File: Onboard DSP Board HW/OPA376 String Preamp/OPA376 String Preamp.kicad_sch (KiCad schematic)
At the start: 4 parts

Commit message: WIP
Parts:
- removed J9: (no value), Connector_JST:JST_SH_SM06B-SRSS-TB_1x06-1MP_P1.00mm_Horizontal, symbol Connector:Conn_01x07_Socket
- added J9: (no value), Connector_PinHeader_2.00mm:PinHeader_1x06_P2.00mm_Horizontal, symbol Connector:Conn_01x06_Pin
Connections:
- net GND: now also J9.1 (Pin_1)
- net SIngle FET preamp/3.3V: now also J9.6 (Pin_6)
- net SIngle FET preamp/Output: now also J9.5 (Pin_5)
- net SIngle FET preamp1/Output: now also J9.4 (Pin_4)
- net SIngle FET preamp2/Output: now also J9.3 (Pin_3)
- net SIngle FET preamp3/Output: now also J9.2 (Pin_2)
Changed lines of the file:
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@@
-	)
-	(junction
-		(at 189.23 93.98)
-		(diameter 0)
-		(color 0 0 0 0)
 	)
 	(junction
@@
 	(wire
 		(pts
-			(xy 194.31 91.44) (xy 189.23 91.44)
-		)
-		(stroke
-			(width 0)
-			(type default)
-		)
-	)
-	(wire
-		(pts
-			(xy 194.31 93.98) (xy 189.23 93.98)
-		)
-		(stroke
-			(width 0)
-			(type default)
-		)
-	)
-	(wire
-		(pts
 			(xy 95.25 58.42) (xy 95.25 68.58)
 		)
@@
 	(wire
 		(pts
+			(xy 194.31 91.44) (xy 193.04 91.44)
+		)
+		(stroke
+			(width 0)
+			(type default)
+		)
+	)
+	(wire
+		(pts
 			(xy 111.76 158.75) (xy 104.14 158.75)
 		)
@@
 	(wire
 		(pts
-			(xy 189.23 93.98) (xy 189.23 96.52)
-		)
-		(stroke
-			(width 0)
-			(type default)
-		)
-	)
-	(wire
-		(pts
 			(xy 85.09 68.58) (xy 85.09 69.85)
 		)
@@
 	(wire
 		(pts
-			(xy 189.23 91.44) (xy 189.23 93.98)
+			(xy 193.04 91.44) (xy 193.04 92.71)
 		)
 		(stroke
@@
 	(symbol
 		(lib_id "power:GND")
-		(at 189.23 96.52 0)
-		(mirror y)
+		(at 193.04 92.71 0)
 		(unit 1)
 		(body_style 1)
@@
 		(dnp no)
 		(fields_autoplaced yes)
-		(property "Reference" "#PWR03"
-			(at 189.23 102.87 0)
+		(property "Reference" "#PWR02"
+			(at 193.04 99.06 0)
 			(hide yes)
 			(show_name no)
@@
 		)
 		(property "Value" "GND"
-			(at 189.23 101.6 0)
+			(at 193.04 97.79 0)
 			(show_name no)
 			(do_not_autoplace no)
@@
 		)
 		(property "Footprint" ""
-			(at 189.23 96.52 0)
+			(at 193.04 92.71 0)
 			(hide yes)
 			(show_name no)
@@
 		)
 		(property "Datasheet" ""
-			(at 189.23 96.52 0)
+			(at 193.04 92.71 0)
 			(hide yes)
 			(show_name no)
@@
 		)
 		(property "Description" "Power symbol creates a global label with name \"GND\" , ground"
-			(at 189.23 96.52 0)
+			(at 193.04 92.71 0)
 			(hide yes)
 			(show_name no)
@@
 			(project "OPA376 String Preamp"
 				(path "/02ac84b2-5c3b-408e-9eb0-8fb87f64ec2b"
-					(reference "#PWR03")
+					(reference "#PWR02")
 					(unit 1)
 				)
@@
 	)
 	(symbol
-		(lib_id "Connector:Conn_01x07_Socket")
-		(at 199.39 86.36 0)
+		(lib_id "Connector:Conn_01x06_Pin")
+		(at 199.39 86.36 180)
 		(unit 1)
 		(body_style 1)
@@
 		(dnp no)
 		(property "Reference" "J9"
-			(at 200.66 85.0899 0)
-			(show_name no)
-			(do_not_autoplace no)
-			(effects
-				(font
-					(size 1.27 1.27)
-				)
-				(justify left)
+			(at 200.66 85.0901 0)
+			(show_name no)
+			(do_not_autoplace no)
+			(effects
+				(font
+					(size 1.27 1.27)
+				)
+				(justify right)
 			)
 		)
 		(property "Value" ""
-			(at 200.66 87.6299 0)
-			(show_name no)
-			(do_not_autoplace no)
-			(effects
-				(font
-					(size 1.27 1.27)
-				)
-				(justify left)
-			)
-		)
-		(property "Footprint" "Connector_JST:JST_SH_SM06B-SRSS-TB_1x06-1MP_P1.00mm_Horizontal"
+			(at 200.66 83.8201 0)
+			(show_name no)
+			(do_not_autoplace no)
+			(effects
+				(font
+					(size 1.27 1.27)
+				)
+				(justify right)
+			)
+		)
+		(property "Footprint" "Connector_PinHeader_2.00mm:PinHeader_1x06_P2.00mm_Horizontal"
 			(at 199.39 86.36 0)
 			(hide yes)
@@
 			)
 		)
-		(property "Description" "Generic connector, single row, 01x07, script generated"
+		(property "Description" "Generic connector, single row, 01x06, script generated"
 			(at 199.39 86.36 0)
 			(hide yes)
@@
 			)
 		)
+		(pin "1"
+		)
 		(pin "5"
 		)
 		(pin "6"
 		)
+		(pin "2"
+		)
+		(pin "3"
+		)
 		(pin "4"
 		)
-		(pin "7"
-		)
-		(pin "3"
-		)
-		(pin "1"
-		)
-		(pin "2"
-		)
 		(instances

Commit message: WIP
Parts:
- C2: value C -> 10uF; footprint Capacitor_SMD:C_0402_1005Metric -> Capacitor_SMD:C_0603_1608Metric
- R1: value R -> 100K
- R2: value R -> 43K
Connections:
- net SIngle FET preamp/3.3V: no longer C2.1
- net SIngle FET preamp/MidRail: now also C2.1
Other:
- moved on the sheet: C2
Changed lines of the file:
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@@
-	)
-	(junction
-		(at 85.09 53.34)
-		(diameter 0)
-		(color 0 0 0 0)
 	)
 	(junction
@@
 	(wire
 		(pts
+			(xy 78.74 68.58) (xy 85.09 68.58)
+		)
+		(stroke
+			(width 0)
+			(type default)
+		)
+	)
+	(wire
+		(pts
 			(xy 104.14 53.34) (xy 111.76 53.34)
 		)
@@
 	(wire
 		(pts
-			(xy 74.93 78.74) (xy 85.09 78.74)
+			(xy 78.74 78.74) (xy 85.09 78.74)
 		)
 		(stroke
@@
 	(wire
 		(pts
-			(xy 74.93 53.34) (xy 74.93 62.23)
-		)
-		(stroke
-			(width 0)
-			(type default)
-		)
-	)
-	(wire
-		(pts
 			(xy 107.95 163.83) (xy 111.76 163.83)
 		)
@@
 	(wire
 		(pts
-			(xy 74.93 69.85) (xy 74.93 78.74)
+			(xy 78.74 77.47) (xy 78.74 78.74)
 		)
 		(stroke
@@
 	(wire
 		(pts
+			(xy 78.74 69.85) (xy 78.74 68.58)
+		)
+		(stroke
+			(width 0)
+			(type default)
+		)
+	)
+	(wire
+		(pts
 			(xy 104.14 71.12) (xy 104.14 87.63)
 		)
@@
 		(pts
 			(xy 107.95 58.42) (xy 95.25 58.42)
-		)
-		(stroke
-			(width 0)
-			(type default)
-		)
-	)
-	(wire
-		(pts
-			(xy 74.93 53.34) (xy 85.09 53.34)
 		)
 		(stroke
@@
 			)
 		)
-		(property "Value" "R"
+		(property "Value" "43K"
 			(at 87.63 74.9299 0)
 			(show_name no)
@@
 	(symbol
 		(lib_id "Device:C")
-		(at 74.93 66.04 0)
+		(at 78.74 73.66 0)
 		(unit 1)
 		(body_style 1)
@@
 		(in_pos_files yes)
 		(dnp no)
-		(fields_autoplaced yes)
 		(property "Reference" "C2"
-			(at 78.74 64.7699 0)
+			(at 71.12 72.3901 0)
 			(show_name no)
 			(do_not_autoplace no)
@@
 			)
 		)
-		(property "Value" "C"
-			(at 78.74 67.3099 0)
+		(property "Value" "10uF"
+			(at 71.12 74.93 0)
 			(show_name no)
 			(do_not_autoplace no)
@@
 			)
 		)
-		(property "Footprint" "Capacitor_SMD:C_0402_1005Metric"
-			(at 75.8952 69.85 0)
+		(property "Footprint" "Capacitor_SMD:C_0603_1608Metric"
+			(at 79.7052 77.47 0)
 			(hide yes)
 			(show_name no)
@@
 		)
 		(property "Datasheet" ""
-			(at 74.93 66.04 0)
+			(at 78.74 73.66 0)
 			(hide yes)
 			(show_name no)
@@
 		)
 		(property "Description" "Unpolarized capacitor"
-			(at 74.93 66.04 0)
+			(at 78.74 73.66 0)
 			(hide yes)
 			(show_name no)
@@
 			)
 		)
-		(property "Value" "R"
+		(property "Value" "100K"
 			(at 87.63 63.4999 0)
 			(show_name no)

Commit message: WIP
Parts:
- J9: now left out of the parts list
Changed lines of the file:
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@@
 		(body_style 1)
 		(exclude_from_sim no)
-		(in_bom yes)
+		(in_bom no)
 		(on_board yes)
 		(in_pos_files yes)

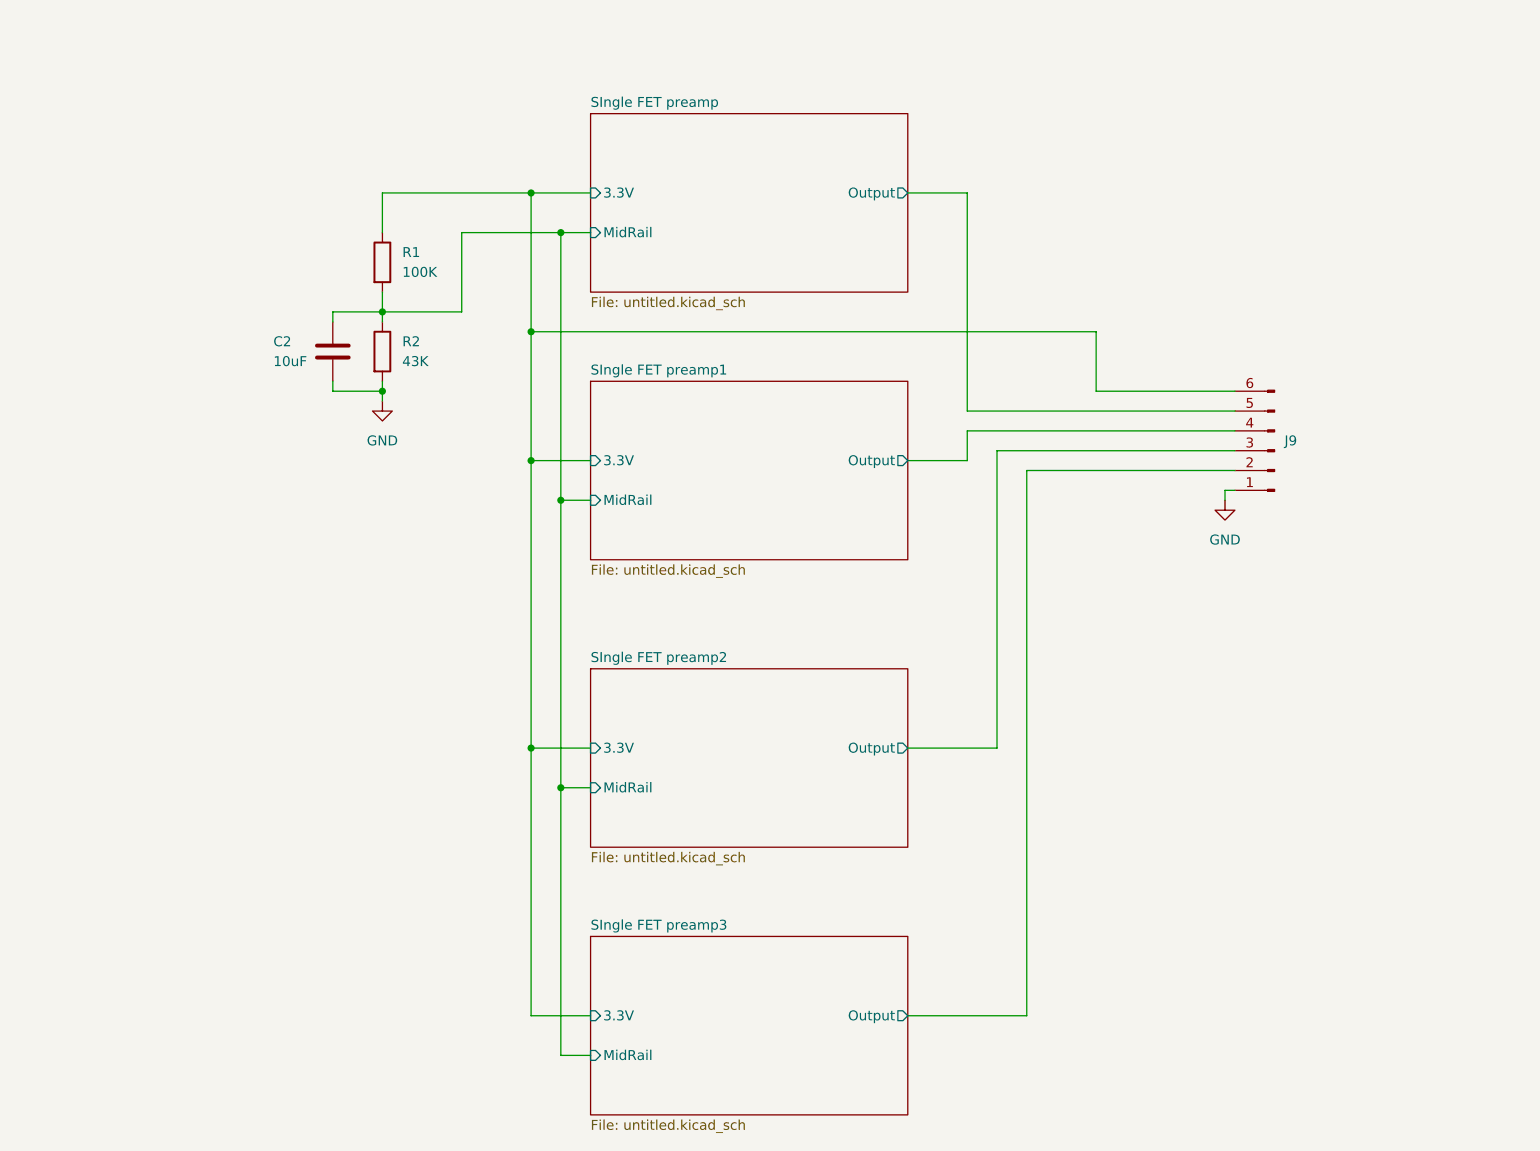
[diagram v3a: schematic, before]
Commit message: Fix Opamp supplies, simulate, add safety resistor to V+
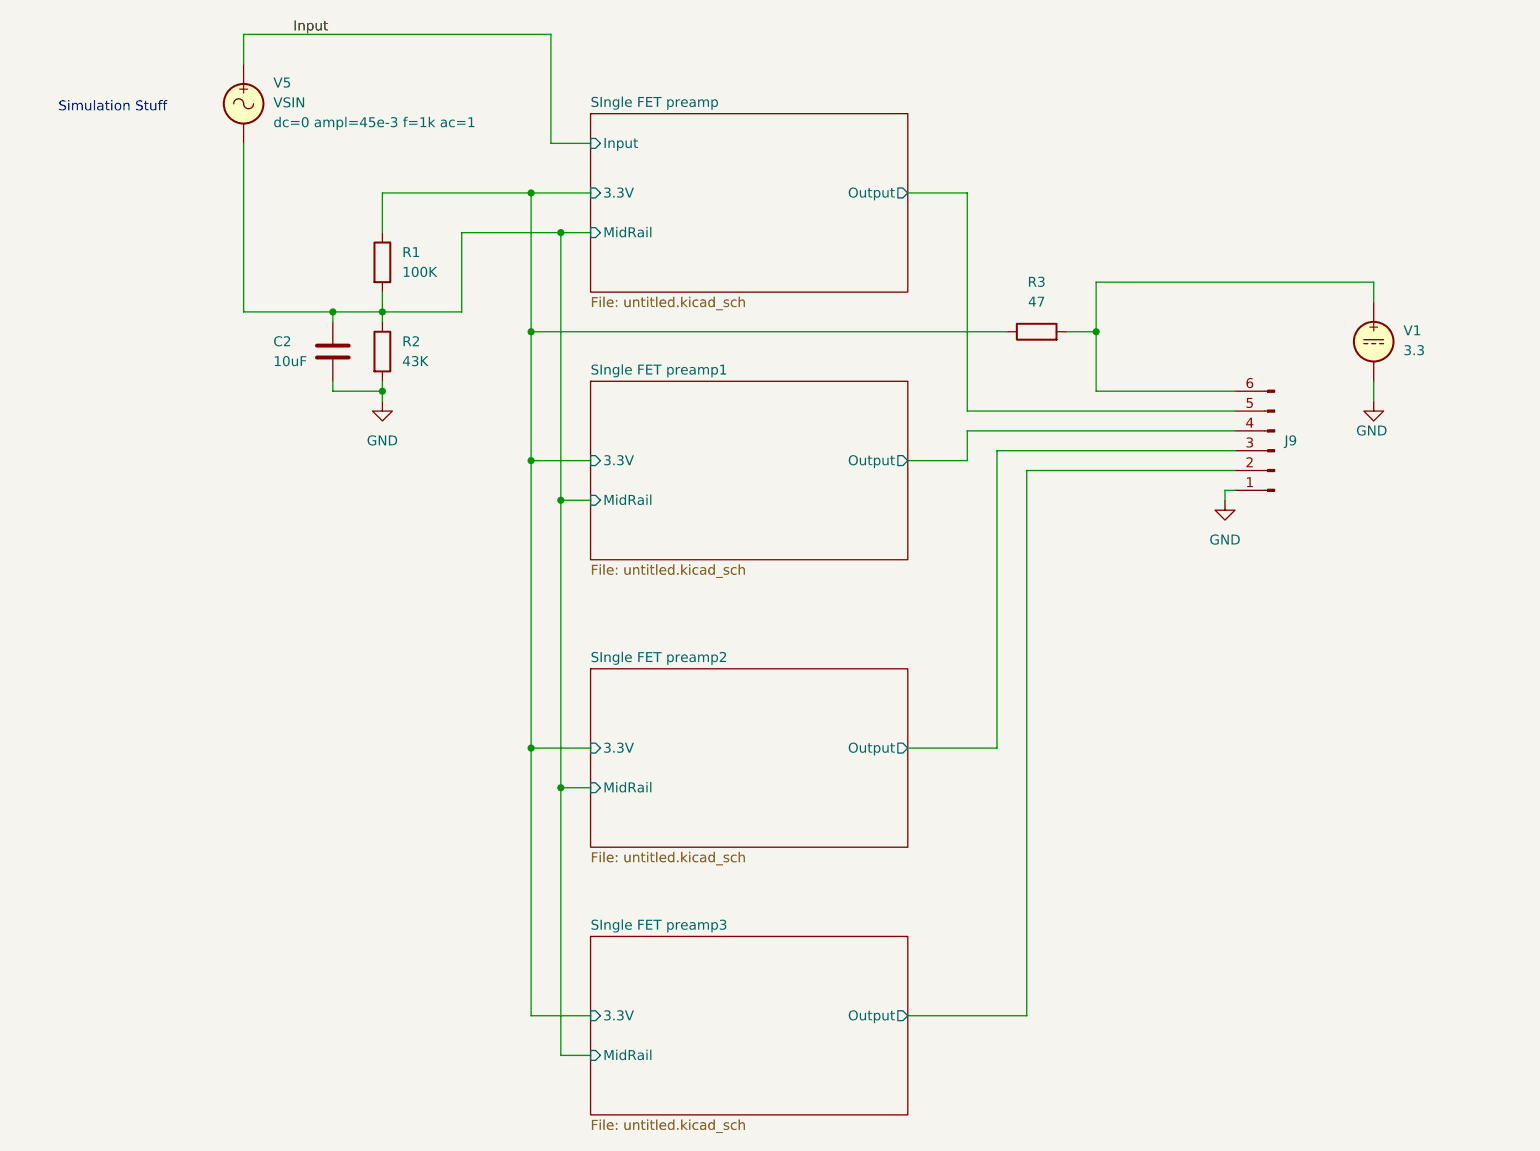
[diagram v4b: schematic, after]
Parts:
- added R3: 47, Resistor_SMD:R_0603_1608Metric, symbol Device:R
- added V1: 3.3, symbol Simulation_SPICE:VDC
- added V5: VSIN, symbol Simulation_SPICE:VSIN
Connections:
- net GND: now also V1.2
- net SIngle FET preamp/3.3V: now also R3.1; no longer J9.6 (Pin_6)
- net SIngle FET preamp/MidRail: now also V5.2
- new net: J9.6 (Pin_6), R3.2, V1.1
- new net Input: V5.1
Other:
- sheet SIngle FET preamp ports: added Input; removed none
- note added: "Simulation Stuff"

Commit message: Add feedback caps damping resistors
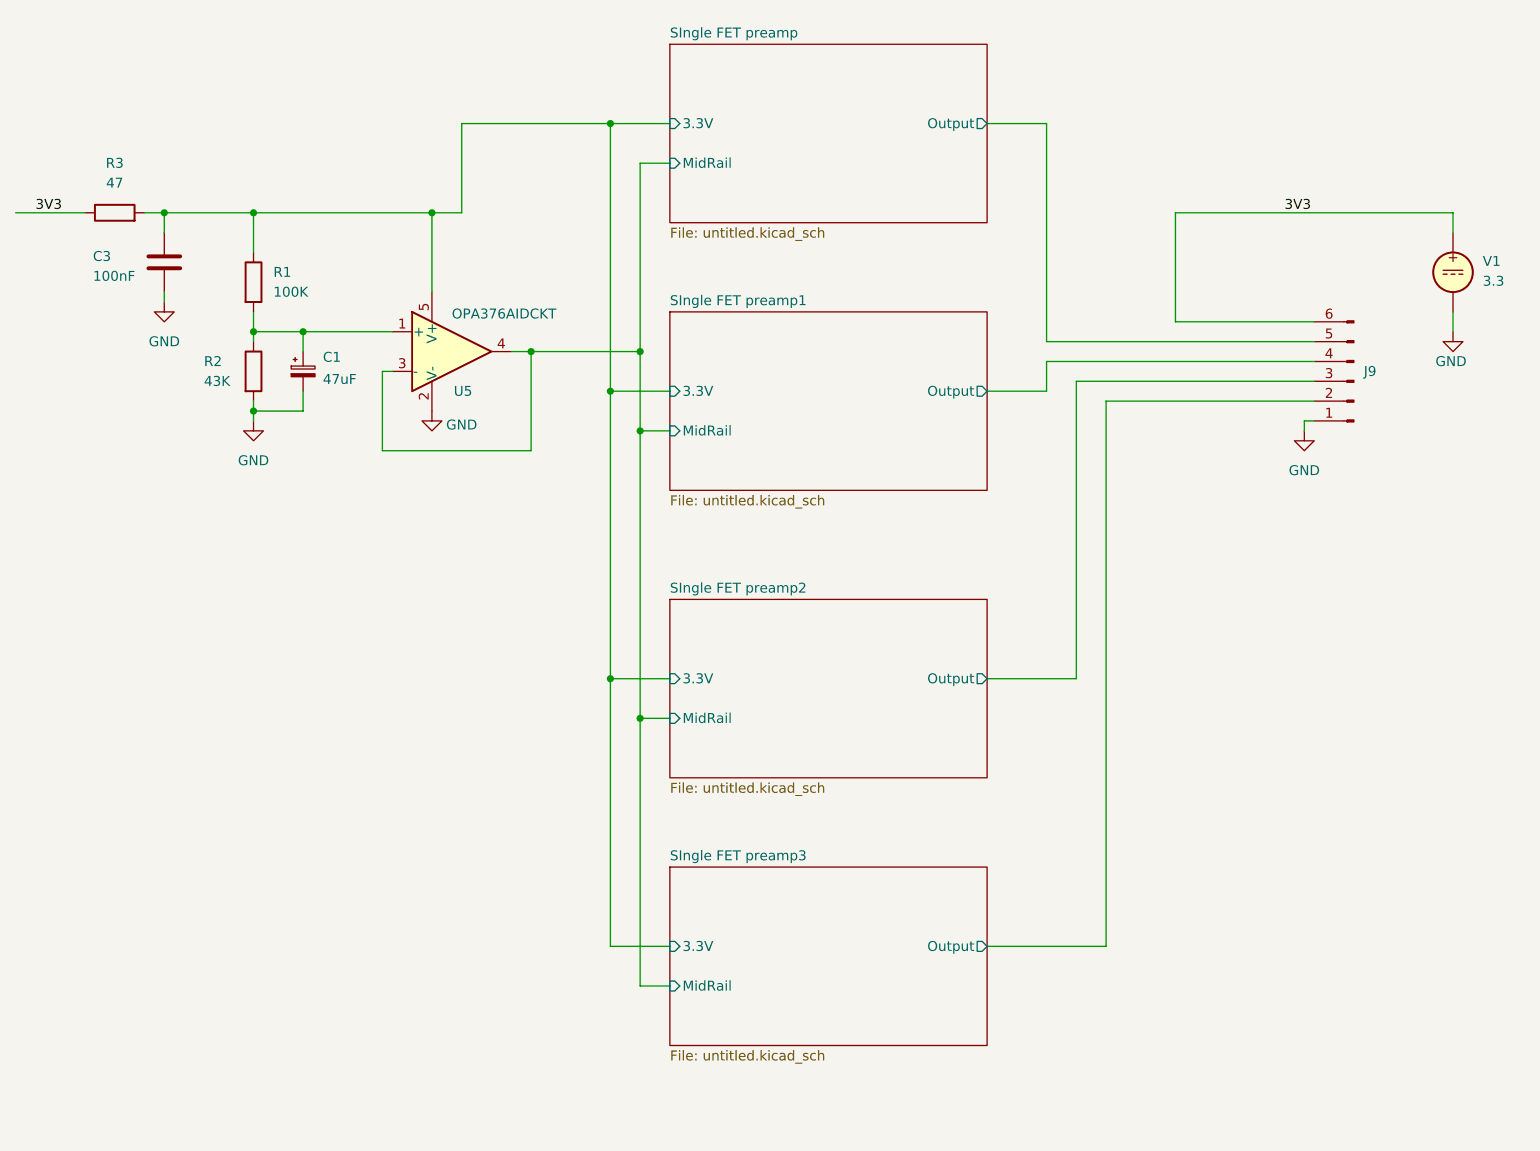
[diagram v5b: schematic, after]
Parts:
- removed C2: 10uF, Capacitor_SMD:C_0603_1608Metric, symbol Device:C
- removed V5: VSIN, symbol Simulation_SPICE:VSIN
- added C1: 47uF, Capacitor_Tantalum_SMD:CP_EIA-3216-12_Kemet-S, symbol Device:C_Polarized_Small
- added C3: 100nF, Capacitor_SMD:C_0603_1608Metric, symbol Device:C
- added U5: OPA376AIDCKT, Package_TO_SOT_SMD:SOT-353_SC-70-5, symbol Amplifier_Operational:OPA376xxDCK
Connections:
- net GND: now also C1.2, C3.2, U5.2 (V-)
- net SIngle FET preamp/3.3V: now also R3.2, C3.1, U5.5 (V+); no longer R3.1
- net SIngle FET preamp/MidRail: now also U5.3 (-), U5.4; no longer R1.2, R2.1
- net 3V3: now reaches J9.6 (Pin_6), V1.1
- net 3V3: now also R3.1; no longer R3.2
- new net: C1.1, R1.2, R2.1, U5.1 (+)
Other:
- sheet SIngle FET preamp ports: added none; removed Input
- note removed: "Simulation Stuff"
- moved on the sheet: J9, R1, R2, R3, V1
